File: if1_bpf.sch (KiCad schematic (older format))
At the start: 10 parts

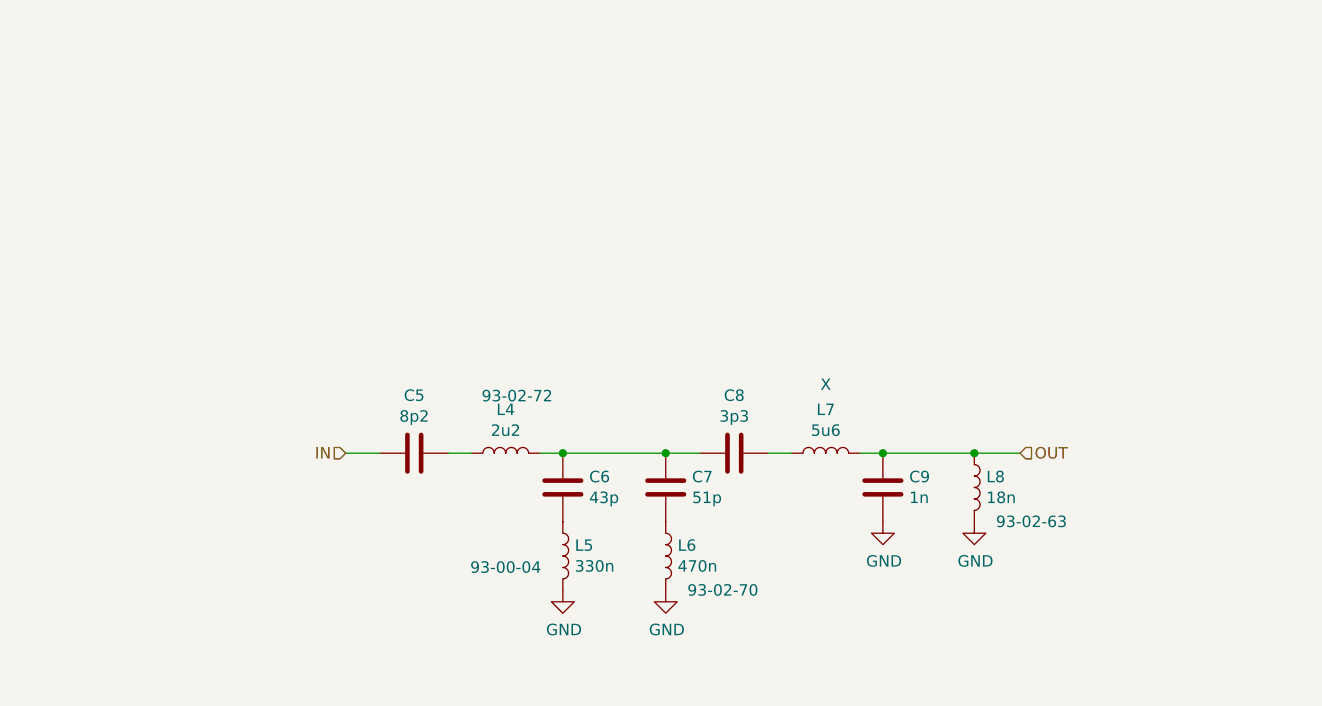
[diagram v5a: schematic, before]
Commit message: if2_bpf revised + Schematic cleanup
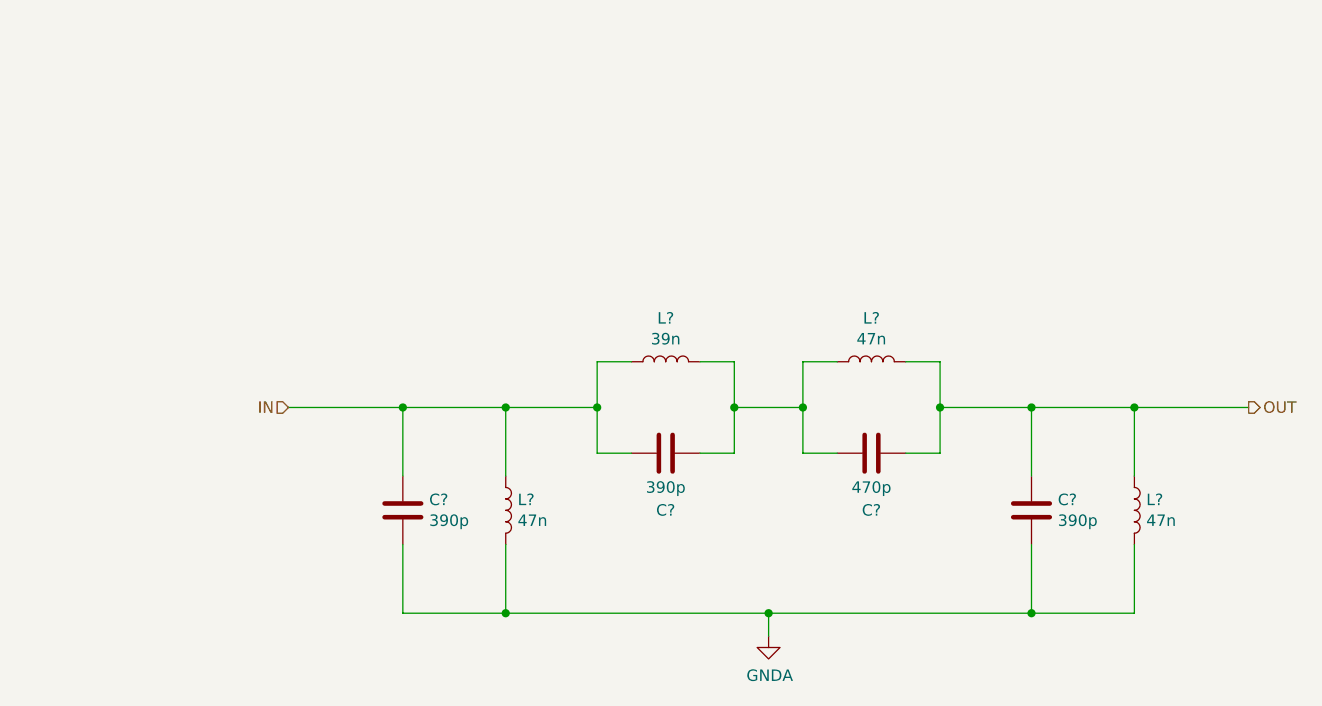
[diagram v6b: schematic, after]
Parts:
- removed C5: 8p2, Capacitor_SMD:C_0805_2012Metric_Pad1.15x1.40mm_HandSolder, symbol Device:C
- removed C6: 43p, Capacitor_SMD:C_0805_2012Metric_Pad1.15x1.40mm_HandSolder, symbol Device:C
- removed C7: 51p, Capacitor_SMD:C_0805_2012Metric_Pad1.15x1.40mm_HandSolder, symbol Device:C
- removed C8: 3p3, Capacitor_SMD:C_0805_2012Metric_Pad1.15x1.40mm_HandSolder, symbol Device:C
- removed C9: 1n, Capacitor_SMD:C_0805_2012Metric_Pad1.15x1.40mm_HandSolder, symbol Device:C
- removed L4: 2u2, Inductor_SMD:L_0805_2012Metric_Pad1.15x1.40mm_HandSolder, symbol Device:L
- removed L5: 330n, Inductor_SMD:L_1210_3225Metric_Pad1.42x2.65mm_HandSolder, symbol Device:L
- removed L6: 470n, Inductor_SMD:L_0805_2012Metric_Pad1.15x1.40mm_HandSolder, symbol Device:L
- removed L7: 5u6, symbol Device:L
- removed L8: 18n, Inductor_SMD:L_0402_1005Metric_Pad0.77x0.64mm_HandSolder, symbol Device:L
- added C? (x3): 390p, symbol Device:C
- added C?: 470p, symbol Device:C
- added L? (x3): 47n, symbol Device:L
- added L?: 39n, symbol Device:L
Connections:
- net IN: now also C?.1, C?.1, L?.1, L?.1
- net OUT: now also C?.1, C?.2, L?.1, L?.2
- new net: C?.1, C?.2, L?.1, L?.2
- new net GNDA: C?.2, C?.2, L?.2, L?.2

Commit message: Footprint reassociation, pcb clear
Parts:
- C5, C6, C7, C8: renamed from C?; footprint (none) -> Capacitor_SMD:C_0805_2012Metric_Pad1.18x1.45mm_HandSolder
- L4, L6, L7: renamed from L?; footprint (none) -> Inductor_SMD:L_0603_1608Metric_Pad1.05x0.95mm_HandSolder
- L5: renamed from L?; footprint (none) -> Inductor_SMD:L_0402_1005Metric_Pad0.77x0.64mm_HandSolder
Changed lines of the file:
@@
 OUT
 $Comp
-L Device:C C?
+L Device:C C5
 U 1 1 600431FC
 P 4450 3850
-F 0 "C?" H 4565 3896 50  0000 L CNN
+F 0 "C5" H 4565 3896 50  0000 L CNN
 F 1 "390p" H 4565 3805 50  0000 L CNN
-F 2 "" H 4488 3700 50  0001 C CNN
+F 2 "Capacitor_SMD:C_0805_2012Metric_Pad1.18x1.45mm_HandSolder" H 4488 3700 50  0001 C CNN
 F 3 "~" H 4450 3850 50  0001 C CNN
 	1    4450 3850
@@
 $EndComp
 $Comp
-L Device:L L?
+L Device:L L4
 U 1 1 600436A2
 P 4900 3850
-F 0 "L?" H 4952 3896 50  0000 L CNN
+F 0 "L4" H 4952 3896 50  0000 L CNN
 F 1 "47n" H 4952 3805 50  0000 L CNN
-F 2 "" H 4900 3850 50  0001 C CNN
+F 2 "Inductor_SMD:L_0603_1608Metric_Pad1.05x0.95mm_HandSolder" H 4900 3850 50  0001 C CNN
 F 3 "~" H 4900 3850 50  0001 C CNN
 F 4 "93-02-59" H 4900 3850 50  0001 C CNN "Lomex"
@@
 $EndComp
 $Comp
-L Device:L L?
+L Device:L L5
 U 1 1 600471E0
 P 5600 3200
-F 0 "L?" V 5790 3200 50  0000 C CNN
+F 0 "L5" V 5790 3200 50  0000 C CNN
 F 1 "39n" V 5699 3200 50  0000 C CNN
-F 2 "" H 5600 3200 50  0001 C CNN
+F 2 "Inductor_SMD:L_0402_1005Metric_Pad0.77x0.64mm_HandSolder" H 5600 3200 50  0001 C CNN
 F 3 "~" H 5600 3200 50  0001 C CNN
 F 4 "2846682RL" H 5600 3200 50  0001 C CNN "Farnell"
@@
 $EndComp
 $Comp
-L Device:C C?
+L Device:C C6
 U 1 1 6004779D
 P 5600 3600
-F 0 "C?" V 5350 3600 50  0000 C CNN
+F 0 "C6" V 5350 3600 50  0000 C CNN
 F 1 "390p" V 5450 3600 50  0000 C CNN
-F 2 "" H 5638 3450 50  0001 C CNN
+F 2 "Capacitor_SMD:C_0805_2012Metric_Pad1.18x1.45mm_HandSolder" H 5638 3450 50  0001 C CNN
 F 3 "~" H 5600 3600 50  0001 C CNN
 	1    5600 3600
@@
 $EndComp
 $Comp
-L Device:L L?
+L Device:L L6
 U 1 1 6004D573
 P 6500 3200
-F 0 "L?" V 6690 3200 50  0000 C CNN
+F 0 "L6" V 6690 3200 50  0000 C CNN
 F 1 "47n" V 6599 3200 50  0000 C CNN
-F 2 "" H 6500 3200 50  0001 C CNN
+F 2 "Inductor_SMD:L_0603_1608Metric_Pad1.05x0.95mm_HandSolder" H 6500 3200 50  0001 C CNN
 F 3 "~" H 6500 3200 50  0001 C CNN
 F 4 "93-02-59" H 6500 3200 50  0001 C CNN "Lomex"
@@
 $EndComp
 $Comp
-L Device:C C?
+L Device:C C7
 U 1 1 6004D579
 P 6500 3600
-F 0 "C?" V 6250 3600 50  0000 C CNN
+F 0 "C7" V 6250 3600 50  0000 C CNN
 F 1 "470p" V 6350 3600 50  0000 C CNN
-F 2 "" H 6538 3450 50  0001 C CNN
+F 2 "Capacitor_SMD:C_0805_2012Metric_Pad1.18x1.45mm_HandSolder" H 6538 3450 50  0001 C CNN
 F 3 "~" H 6500 3600 50  0001 C CNN
 	1    6500 3600
@@
 $EndComp
 $Comp
-L Device:C C?
+L Device:C C8
 U 1 1 6004E74D
 P 7200 3850
-F 0 "C?" H 7315 3896 50  0000 L CNN
+F 0 "C8" H 7315 3896 50  0000 L CNN
 F 1 "390p" H 7315 3805 50  0000 L CNN
-F 2 "" H 7238 3700 50  0001 C CNN
+F 2 "Capacitor_SMD:C_0805_2012Metric_Pad1.18x1.45mm_HandSolder" H 7238 3700 50  0001 C CNN
 F 3 "~" H 7200 3850 50  0001 C CNN
 	1    7200 3850
@@
 $EndComp
 $Comp
-L Device:L L?
+L Device:L L7
 U 1 1 6004E753
 P 7650 3850
-F 0 "L?" H 7702 3896 50  0000 L CNN
+F 0 "L7" H 7702 3896 50  0000 L CNN
 F 1 "47n" H 7702 3805 50  0000 L CNN
-F 2 "" H 7650 3850 50  0001 C CNN
+F 2 "Inductor_SMD:L_0603_1608Metric_Pad1.05x0.95mm_HandSolder" H 7650 3850 50  0001 C CNN
 F 3 "~" H 7650 3850 50  0001 C CNN
 F 4 "93-02-59" H 7650 3850 50  0001 C CNN "Lomex"
@@
 	6050 4300 7200 4300
 $Comp
-L power:GNDA #PWR?
+L power:GNDA #PWR0108
 U 1 1 60071173
 P 6050 4400
-F 0 "#PWR?" H 6050 4150 50  0001 C CNN
+F 0 "#PWR0108" H 6050 4150 50  0001 C CNN
 F 1 "GNDA" H 6055 4227 50  0000 C CNN
 F 2 "" H 6050 4400 50  0001 C CNN
